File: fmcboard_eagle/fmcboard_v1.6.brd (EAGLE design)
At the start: 147 x 74 mm, 239 parts, among them IC1 OPA695IDR, IC10 LM358, IC11 7805DT, IC12 SN74AUC2G66DCTR, IC13 SN74AUC2G66DCTR, IC14 SN74AUC2G66DCTR, IC15 SN74AUC2G66DCTR, IC16 DAC7578SPWR, IC17 SN74AUC2G66DCTR, IC18 SN74AUC2G66DCTR, IC19 SN74AUC2G66DCTR, IC2 DAC7578SPWR, IC20 SN74AUC2G66DCTR, IC21 74AUP2GU04GW, IC22 74AUP2GU04GW, IC23 74AUP2GU04GW, IC24 74AUP2GU04GW, IC25 MC7905ACD2TR4G, IC26 AMS1117-1.8, IC27 OPA699ID, IC29 LM337KVURG3, IC3 LTC6229IMS8E#TRPBF, IC4 OPA695IDR, IC5 LTC6229IMS8E#TRPBF, IC6 OPA695IDR, IC7 OPA699ID, IC8 LM358, IC9 LM358, J1 8pin, J11 4p-2.54, J12 4p-2.54, J13 4p-2.54, J14 4p-2.54, J2 ASP-134604-01, J3 4p-2.54, J4 4p-2.54, J5 4p-2.54, J6 4p-2.54, J7 4p-2.54, J8 4p-2.54, J9 8pin, U1 TXS0108EPWR

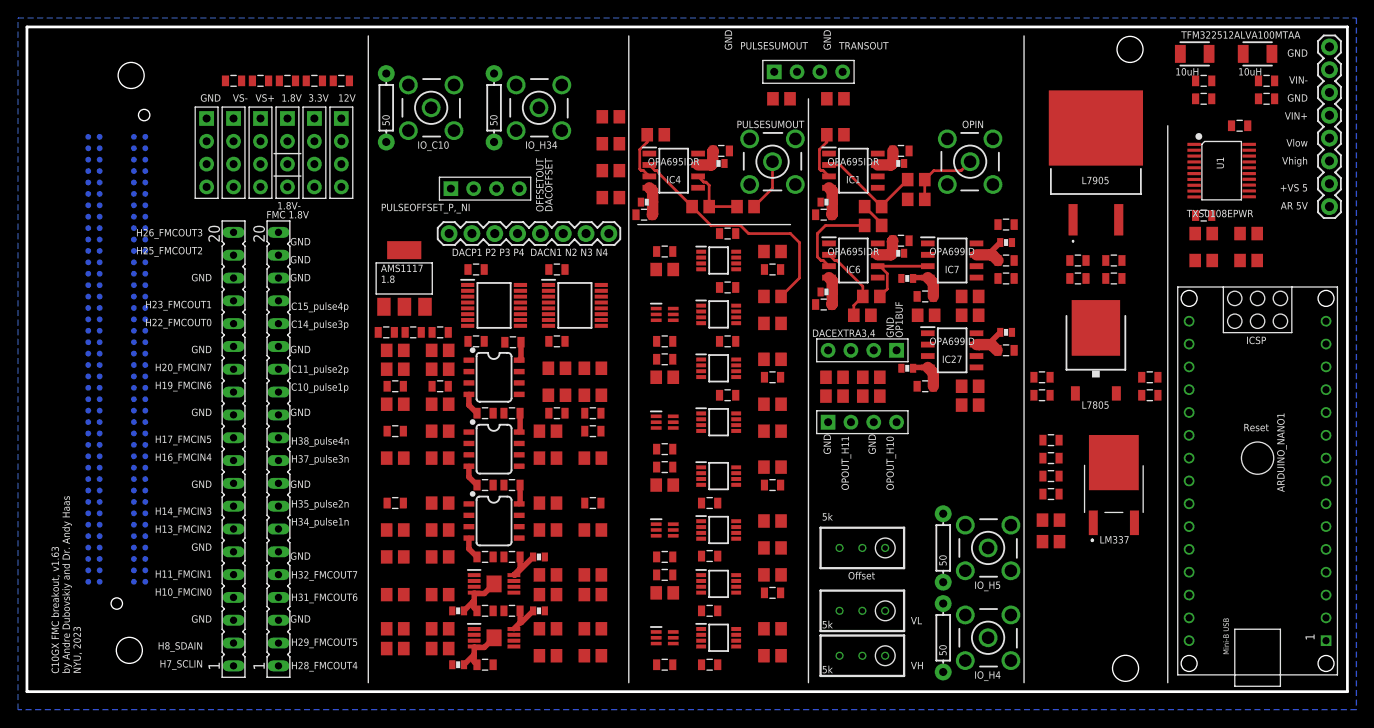
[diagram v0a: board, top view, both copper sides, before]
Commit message: Power routed
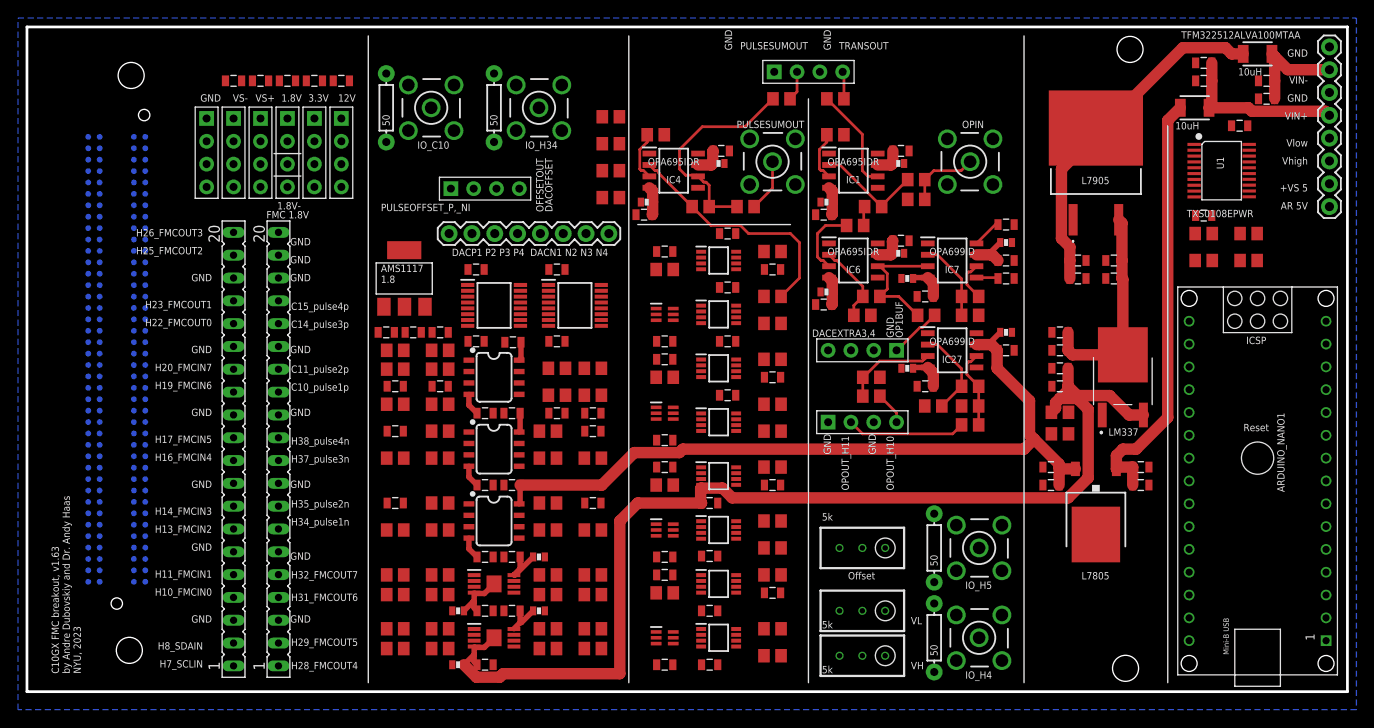
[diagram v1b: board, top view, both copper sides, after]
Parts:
- moved IC11 18.0 mm to (119.0, 20.0), turned to 180 degrees
- moved R78 15.4 mm to (105.0, 29.7), turned to 0 degrees
- moved R87 15.4 mm to (105.0, 31.8), turned to 0 degrees
- moved C2 14.9 mm to (124.0, 23.0), turned to 0 degrees
- moved C38 14.9 mm to (114.0, 25.0), turned to 180 degrees
- moved C43 14.9 mm to (124.0, 25.0), turned to 0 degrees
- moved C47 14.9 mm to (114.0, 23.0), turned to 180 degrees
- moved C33 12.0 mm to (115.0, 38.0)
- moved C65 12.0 mm to (115.0, 36.0)
- moved C77 12.0 mm to (115.0, 40.0)
- moved C86 12.0 mm to (115.0, 34.0)
- moved IC29 12.0 mm to (122.0, 35.0)
- moved R14 12.0 mm to (115.0, 31.1)
- moved R70 12.0 mm to (115.0, 28.7)
- moved L1 6.00 mm to (130.0, 65.0)
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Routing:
- net 1V8-: track 12.5 -> 130.4 mm
- net VS+: track 36.6 -> 115.7 mm
- net VIN+CLEAN: track 0.00 -> 47.9 mm
- net VIN-CLEAN: track 0.00 -> 38.7 mm
- net VS-: track 25.0 -> 48.5 mm
- net VIN+: track 0.00 -> 18.9 mm
- net PULSESUMOUT: track 7.12 -> 24.5 mm
- net OPOUT_H10: track 0.00 -> 14.8 mm
- net N$40: track 0.00 -> 13.3 mm
- net VIN-: track 0.00 -> 11.8 mm
- net TRANSOUT: track 2.89 -> 13.8 mm
- net N$1: track 0.00 -> 9.93 mm
- net N$11: track 0.00 -> 8.92 mm
- net OPOUT_H11: track 0.00 -> 8.80 mm
- net N$42: track 0.00 -> 5.86 mm
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
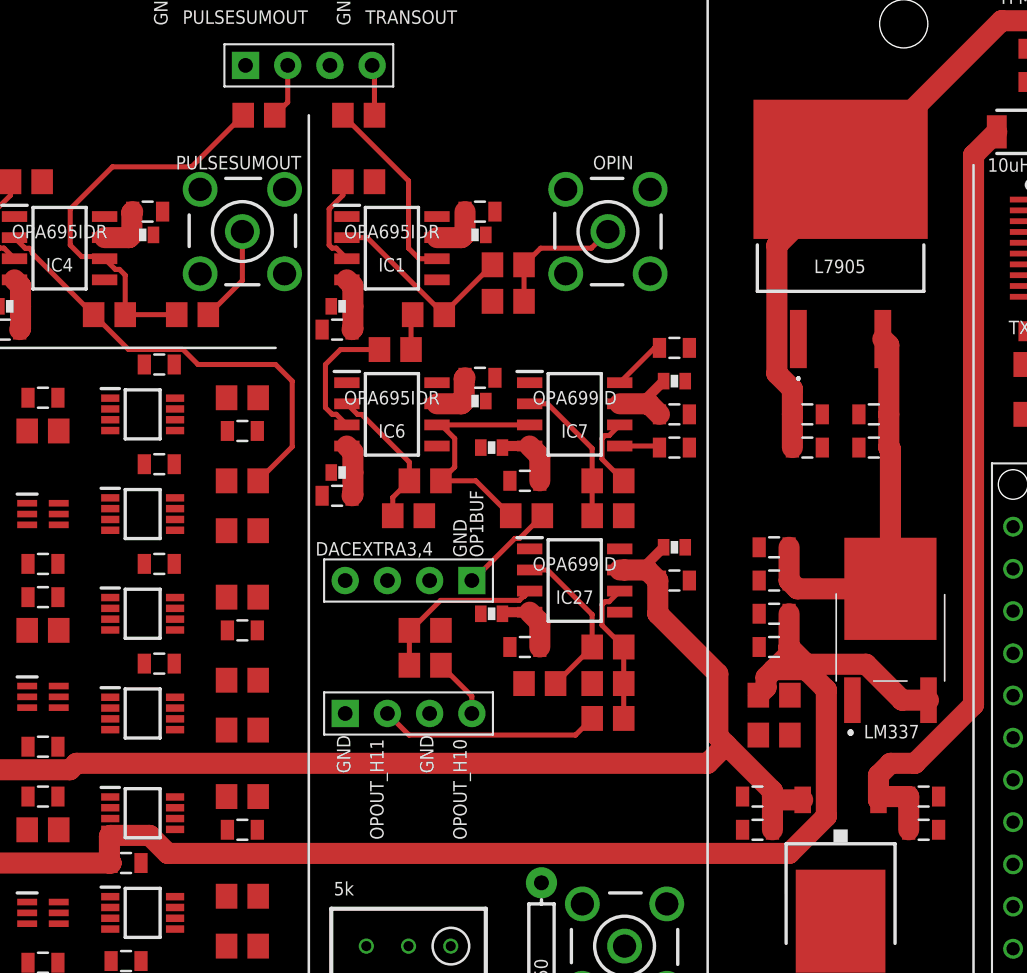
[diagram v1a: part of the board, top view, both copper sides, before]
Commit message: Better 7805 7905 footprints
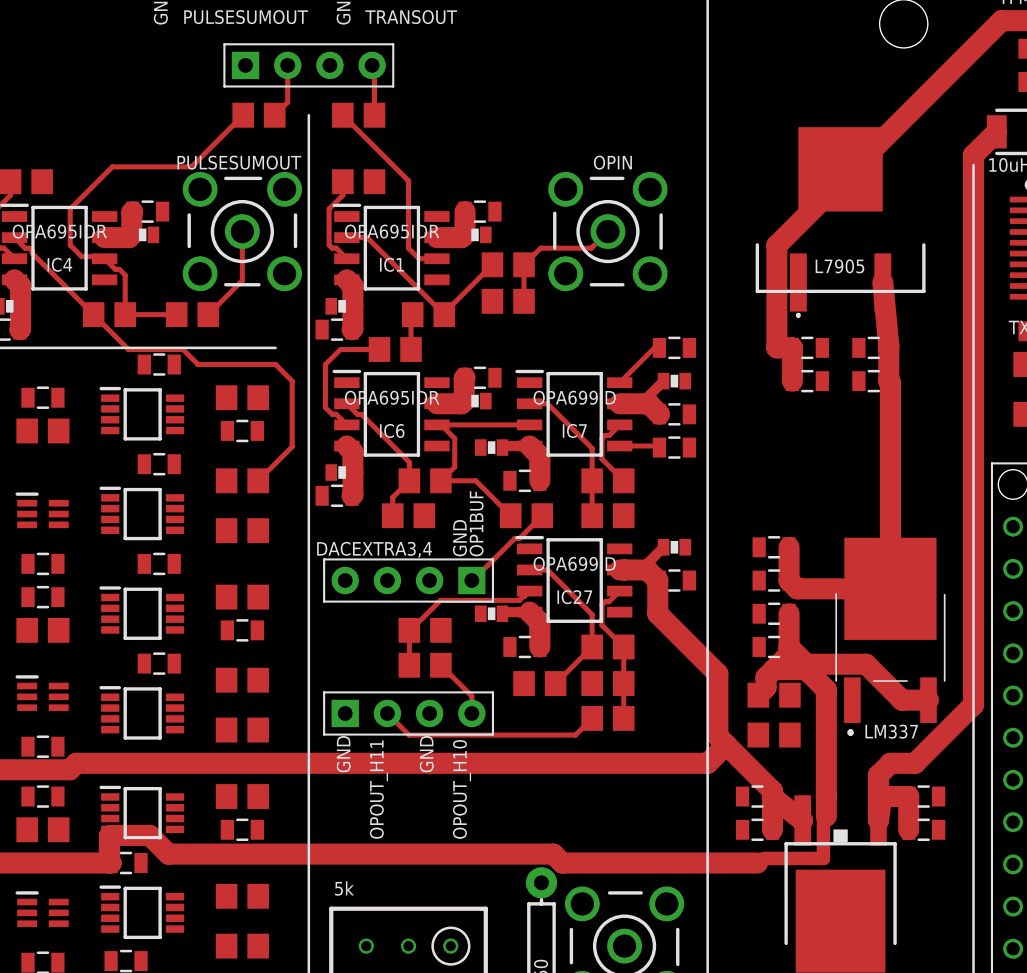
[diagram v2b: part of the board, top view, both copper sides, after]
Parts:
- moved C25 4.00 mm to (121.0, 52.0)
- moved C39 4.00 mm to (121.0, 50.0)
- moved C40 4.00 mm to (117.0, 50.0)
- moved C45 4.00 mm to (117.0, 52.0)
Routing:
- net VIN-CLEAN: track 38.7 -> 35.2 mm
- net VS-: track 48.5 -> 51.8 mm
- net 1V8-: track 130.4 -> 133.5 mm
- net VIN+CLEAN: track 47.9 -> 50.3 mm

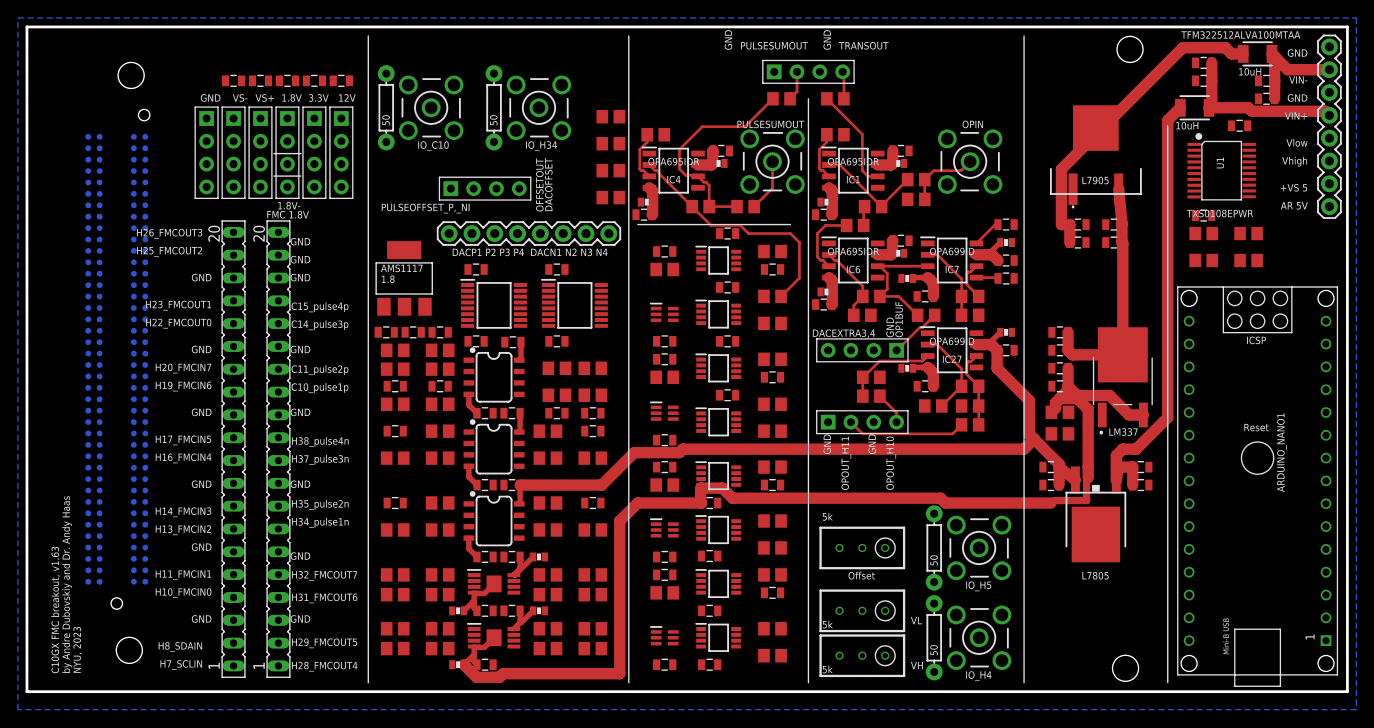
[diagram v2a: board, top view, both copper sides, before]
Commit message: mostly routed
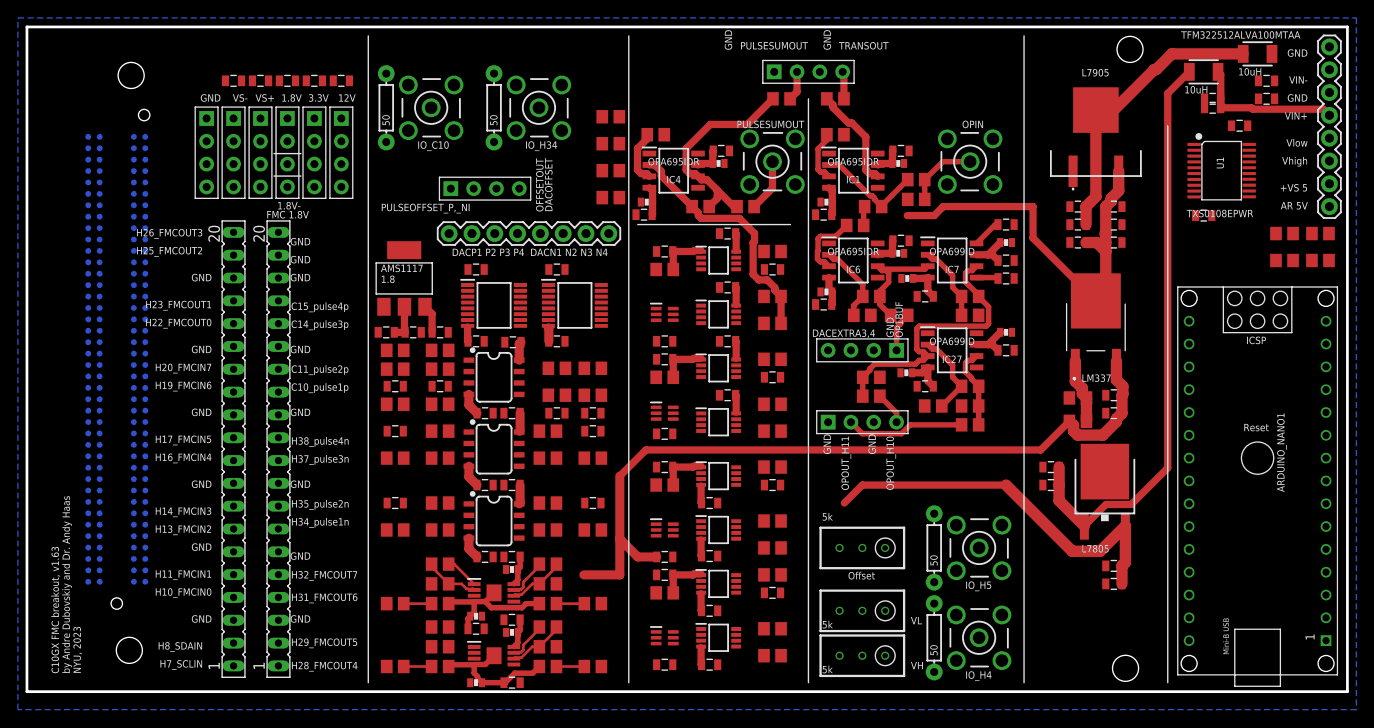
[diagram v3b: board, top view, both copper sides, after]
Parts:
- R17: value 100k -> 4.7k
- R42: value 10k -> 4.7k
- moved C38 14.8 mm to (121.0, 12.0)
- moved C33 13.4 mm to (121.0, 50.0), turned to 0 degrees
- moved C47 11.4 mm to (121.0, 14.0)
- moved C77 10.2 mm to (117.0, 50.0)
- moved C2 10.0 mm to (114.0, 23.0), turned to 180 degrees
- moved C43 10.0 mm to (114.0, 25.0), turned to 180 degrees
- moved R49 9.00 mm to (140.0, 48.0)
- moved R51 9.00 mm to (140.0, 51.0)
- moved R48 8.00 mm to (144.0, 48.0)
- moved R50 8.00 mm to (144.0, 51.0)
- moved C65 6.71 mm to (121.0, 33.0)
- moved C86 6.71 mm to (121.0, 31.0)
- moved IC29 6.71 mm to (119.0, 41.0)
- moved R23 5.14 mm to (46.0, 14.2), turned to 180 degrees
- moved R29 5.14 mm to (58.0, 14.2), turned to 180 degrees
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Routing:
- net VS+: track 116.1 -> 79.2 mm
- net VS-: track 51.8 -> 71.3 mm
- net OPOUT_H10: track 14.8 -> 30.7 mm
- net VIN+CLEAN: track 50.3 -> 64.8 mm
- net 1V8: track 0.00 -> 13.2 mm
- net VIN-: track 11.8 -> 0.00 mm
- net 1V8-: track 133.5 -> 124.6 mm
- net N$30: track 0.00 -> 7.21 mm
- net N$12: track 0.00 -> 6.37 mm
- net N$4: track 0.00 -> 6.37 mm
- net N$13: track 0.00 -> 6.10 mm
- net DACP3: track 0.00 -> 5.22 mm
- net DACP1: track 0.00 -> 5.22 mm
- net DACN3I: track 0.00 -> 5.22 mm
- net DACN1I: track 0.00 -> 5.22 mm
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
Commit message: routed v1.63
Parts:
- moved R26 2.00 mm to (103.0, 41.9), turned to 0 degrees
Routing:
- net GND: track 0.00 -> 632.9 mm, vias 0 -> 37
- net VS+: track 79.2 -> 391.8 mm, vias 0 -> 8
- net 1V8: track 13.2 -> 218.4 mm, vias 0 -> 5
- net VS-: track 71.3 -> 268.2 mm, vias 0 -> 11
- net SDAIN: track 0.00 -> 189.7 mm, vias 0 -> 3
- net AR_SCLIN2: track 0.00 -> 183.8 mm, vias 0 -> 5
- net SCLIN: track 0.00 -> 163.7 mm, vias 0 -> 2
- net H35: track 0.00 -> 161.1 mm, vias 0 -> 5
- net 1V8-: track 124.6 -> 278.4 mm, vias 0 -> 3
- net H38: track 0.00 -> 153.7 mm, vias 0 -> 7
- net AR_SDAIN2: track 0.00 -> 151.5 mm, vias 0 -> 8
- net H37: track 0.00 -> 138.7 mm, vias 0 -> 3
- net G37: track 0.00 -> 133.3 mm, vias 0 -> 4
- net G36: track 0.00 -> 132.7 mm, vias 0 -> 4
- net C10: track 0.00 -> 132.2 mm, vias 0 -> 10
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
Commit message: routed v1.63
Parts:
- moved C1 1.00 mm to (132.0, 64.0)
- moved C6 1.00 mm to (136.0, 63.0)
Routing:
- net GND: track 632.9 -> 634.2 mm
- net VIN+: track 16.6 -> 17.9 mm
- net VS+: track 391.8 -> 390.6 mm
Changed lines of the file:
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@@
 <attribute name="MPN" value="F185-1104A1BSYA1" x="16" y="71" size="1.778" layer="27" display="off"/>
 </element>
-<element name="C6" library="SparkFun-Passives" package="0805" value="0.1uF" x="135" y="63" smashed="yes" rot="R180"/>
+<element name="C6" library="SparkFun-Passives" package="0805" value="0.1uF" x="136" y="63" smashed="yes" rot="R180"/>
 <element name="C15" library="SparkFun-Passives" package="0805" value="0.1uF" x="51" y="31" smashed="yes"/>
 <element name="C16" library="SparkFun-Passives" package="0805" value="0.1uF" x="77.3" y="60.2" smashed="yes"/>
@@
 <attribute name="SPICEPREFIX" value="R" x="140" y="51" size="1.778" layer="27" rot="R180" display="off"/>
 </element>
-<element name="C1" library="SparkFun-Passives" package="0805" value="10uF" x="132" y="65" smashed="yes" rot="R180"/>
+<element name="C1" library="SparkFun-Passives" package="0805" value="10uF" x="132" y="64" smashed="yes" rot="R180"/>
 <element name="C2" library="SparkFun-Passives" package="0805" value="10uF" x="114" y="23" smashed="yes" rot="R180"/>
 <element name="C38" library="SparkFun-Passives" package="0805" value="10uF" x="121" y="12" smashed="yes" rot="R180"/>
@@
 <wire x1="39" y1="34.375" x2="39" y2="38.875" width="0.3048" layer="1"/>
 <wire x1="39.125" y1="39.875" x2="39.1" y2="40" width="0.3048" layer="1"/>
-<wire x1="131.125" y1="66" x2="131.125" y2="65" width="0.3048" layer="1"/>
-<wire x1="131.125" y1="65" x2="131.1" y2="65" width="0.3048" layer="1"/>
+<wire x1="131.125" y1="66" x2="131.125" y2="64" width="0.3048" layer="1"/>
+<wire x1="131.125" y1="64" x2="131.1" y2="64" width="0.3048" layer="1"/>
 <wire x1="131.125" y1="66" x2="131.1" y2="66" width="0.3048" layer="1"/>
 <wire x1="132" y1="61" x2="132" y2="57.25" width="0.3048" layer="1"/>
 <wire x1="132" y1="57.25" x2="132" y2="53" width="0.3048" layer="1"/>
-<wire x1="134" y1="63" x2="133.625" y2="62.625" width="0.3048" layer="1"/>
-<wire x1="133.625" y1="62.625" x2="132" y2="61" width="0.3048" layer="1"/>
+<wire x1="134" y1="63" x2="133.125" y2="62.125" width="0.3048" layer="1"/>
+<wire x1="133.125" y1="62.125" x2="132" y2="61" width="0.3048" layer="1"/>
 <wire x1="132" y1="53" x2="131.9" y2="53" width="0.3048" layer="1"/>
-<wire x1="134" y1="63" x2="134.1" y2="63" width="0.3048" layer="1"/>
-<wire x1="133.625" y1="62.625" x2="131.25" y2="65" width="0.3048" layer="1"/>
-<wire x1="131.25" y1="65" x2="131.1" y2="65" width="0.3048" layer="1"/>
+<wire x1="134" y1="63" x2="135.1" y2="63" width="0.3048" layer="1"/>
+<wire x1="133.125" y1="62.125" x2="131.25" y2="64" width="0.3048" layer="1"/>
+<wire x1="131.25" y1="64" x2="131.1" y2="64" width="0.3048" layer="1"/>
 <wire x1="88.25" y1="53.5" x2="88.25" y2="54.5" width="0.3048" layer="1"/>
 <wire x1="87.875" y1="53.125" x2="88.25" y2="53.5" width="0.3048" layer="1"/>
@@
 <wire x1="76.75" y1="60.375" x2="76.4" y2="60.2" width="0.4064" layer="1"/>
 <wire x1="96.125" y1="60.25" x2="96.4" y2="60.2" width="0.4064" layer="1"/>
-<wire x1="135.875" y1="62.25" x2="135.875" y2="63" width="0.4064" layer="1"/>
-<wire x1="134.875" y1="61.25" x2="135.875" y2="62.25" width="0.4064" layer="1"/>
-<wire x1="134.875" y1="60.625" x2="134.875" y2="61.25" width="0.4064" layer="1"/>
-<wire x1="135.125" y1="60.375" x2="134.875" y2="60.625" width="0.4064" layer="1"/>
-<wire x1="136" y1="60.375" x2="135.125" y2="60.375" width="0.4064" layer="1"/>
-<wire x1="135.875" y1="63" x2="135.9" y2="63" width="0.4064" layer="1"/>
-<wire x1="136" y1="60.375" x2="136.065" y2="60.275" width="0.4064" layer="1"/>
-<wire x1="141.375" y1="60.25" x2="136.25" y2="60.25" width="0.4064" layer="1"/>
+<wire x1="141.375" y1="60.25" x2="138" y2="60.25" width="0.4064" layer="1"/>
+<wire x1="138" y1="60.25" x2="136.25" y2="60.25" width="0.4064" layer="1"/>
 <wire x1="145" y1="56.625" x2="141.375" y2="60.25" width="0.4064" layer="1"/>
-<wire x1="136.25" y1="60.25" x2="136.065" y2="60.275" width="0.4064" layer="1"/>
 <wire x1="145" y1="56.625" x2="145" y2="56.54" width="0.4064" layer="1"/>
 <wire x1="90.375" y1="7.875" x2="90.375" y2="4" width="0.4064" layer="1"/>
@@
 <via x="103.875" y="53.125" extent="1-16" drill="0.3048"/>
 <via x="54" y="5.75" extent="1-16" drill="0.3048"/>
+<wire x1="136.9" y1="63" x2="138" y2="61.9" width="0.4064" layer="1"/>
+<wire x1="138" y1="61.9" x2="138" y2="60.25" width="0.4064" layer="1"/>
+<wire x1="136.25" y1="60.25" x2="136.065" y2="60.275" width="0" layer="19" extent="1-1"/>
 </signal>
 <signal name="VS-" class="1" airwireshidden="yes">
@@
 <wire x1="132.6" y1="69" x2="132.9" y2="68.7" width="0.8128" layer="1"/>
 <wire x1="132.9" y1="68.7" x2="132.9" y2="66" width="0.8128" layer="1"/>
-<wire x1="132.9" y1="66" x2="132.9" y2="65" width="0.8128" layer="1"/>
-<wire x1="132.9" y1="65" x2="136.3097375" y2="65" width="0.8128" layer="1"/>
-<wire x1="136.3097375" y1="65" x2="136.4685375" y2="64.8412" width="0.8128" layer="1"/>
+<wire x1="132.9" y1="66" x2="132.9" y2="64" width="0.8128" layer="1"/>
+<wire x1="144.3188" y1="64.8412" x2="133.7412" y2="64.8412" width="0.8128" layer="1"/>
+<wire x1="132.9" y1="64" x2="133.7412" y2="64.8412" width="0.8128" layer="1"/>
 <wire x1="144.3188" y1="64.8412" x2="145" y2="64.16" width="0.8128" layer="1"/>
-<wire x1="136.4685375" y1="64.8412" x2="144.3188" y2="64.8412" width="0.8128" layer="1"/>
 </signal>
 <signal name="VIN-" class="1">
